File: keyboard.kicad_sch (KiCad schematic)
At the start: 31 parts, among them SW1 SW_PUSH, SW10 SW_PUSH, SW11 SW_PUSH, SW12 SW_PUSH, SW13 SW_PUSH, SW14 SW_PUSH, SW15 SW_PUSH, SW16 SW_PUSH, SW17 SW_PUSH, SW18 SW_PUSH, SW19 SW_PUSH, SW2 SW_PUSH, SW20 SW_PUSH, SW21 SW_PUSH, SW22 SW_PUSH, SW23 SW_PUSH, SW24 SW_PUSH, SW25 SW_PUSH, SW26 SW_PUSH, SW3 SW_PUSH, SW4 SW_PUSH, SW5 SW_PUSH, SW6 SW_PUSH, SW7 SW_PUSH, SW8 SW_PUSH, SW9 SW_PUSH

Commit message: Approximate layout
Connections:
- net SW01L: now also YJT1.2 (P21), YJT2.35 (P19); no longer YJT1.9 (P28), YJT2.9 (P28)
- net SW02L: now also YJT1.14 (P00), YJT2.23 (P09); no longer YJT1.4 (P23), YJT2.4 (P23)
- net SW03L: now also YJT1.20 (P06), YJT2.17 (P03); no longer YJT1.3 (P22), YJT2.3 (P22)
- net SW04L: now also YJT1.26 (P12), YJT2.26 (P12); no longer YJT1.2 (P21), YJT2.2 (P21)
- net SW05L: now also YJT1.3 (P22), YJT2.34 (P18); no longer YJT1.27 (P13), YJT2.27 (P13)
- net SW06L: now also YJT1.15 (P01), YJT2.22 (P08); no longer YJT1.24 (P10), YJT2.24 (P10)
- net SW07L: now also YJT1.21 (P07), YJT2.16 (P02); no longer YJT1.23 (P09), YJT2.23 (P09)
- net SW08L: now also YJT1.27 (P13), YJT2.10 (P29); no longer YJT1.22 (P08), YJT2.22 (P08)
- net SW09L: now also YJT1.4 (P23), YJT2.33 (P17); no longer YJT1.26 (P12), YJT2.26 (P12)
- net SW10L: now also YJT1.16 (P02), YJT2.21 (P07); no longer YJT1.17 (P03), YJT2.17 (P03)
- net SW11L: now also YJT1.22 (P08), YJT2.15 (P01); no longer YJT1.16 (P02), YJT2.16 (P02)
- net SW12L: now also YJT1.28 (P14), YJT2.9 (P28); no longer YJT1.15 (P01), YJT2.15 (P01)
- net SW13L: now also YJT1.9 (P28), YJT2.28 (P14); no longer YJT1.14 (P00), YJT2.14 (P00)
- net SW14L: now also YJT1.17 (P03), YJT2.20 (P06); no longer YJT1.13 (P30), YJT2.13 (P30)
- net SW15L: now also YJT1.23 (P09), YJT2.14 (P00); no longer YJT1.25 (P11), YJT2.25 (P11)
- net SW16L: now also YJT1.29 (P15), YJT2.29 (P15); no longer YJT1.28 (P14), YJT2.28 (P14)
- net SW17L: now also YJT1.10 (P29), YJT2.27 (P13); no longer YJT1.29 (P15), YJT2.29 (P15)
- net SW18L: now also YJT1.18 (P04), YJT2.19 (P05); no longer YJT1.30 (P16), YJT2.30 (P16)
- net SW19L: now also YJT1.24 (P10), YJT2.13 (P30); no longer YJT1.33 (P17), YJT2.33 (P17)
- net SW20L: now also YJT1.30 (P16), YJT2.30 (P16); no longer YJT1.18 (P04), YJT2.18 (P04)
- net SW21L: now also YJT1.13 (P30), YJT2.24 (P10); no longer YJT1.19 (P05), YJT2.19 (P05)
- net SW22L: now also YJT1.19 (P05), YJT2.18 (P04); no longer YJT1.20 (P06), YJT2.20 (P06)
- net SW23L: now also YJT1.25 (P11), YJT2.25 (P11); no longer YJT1.21 (P07), YJT2.21 (P07)
- net SW24L: now also YJT1.33 (P17), YJT2.4 (P23); no longer YJT1.34 (P18), YJT2.34 (P18)
- net SW25L: now also YJT1.34 (P18), YJT2.3 (P22); no longer YJT1.35 (P19), YJT2.35 (P19)
- net SW26L: now also YJT1.35 (P19), YJT2.2 (P21); no longer YJT1.10 (P29), YJT2.10 (P29)

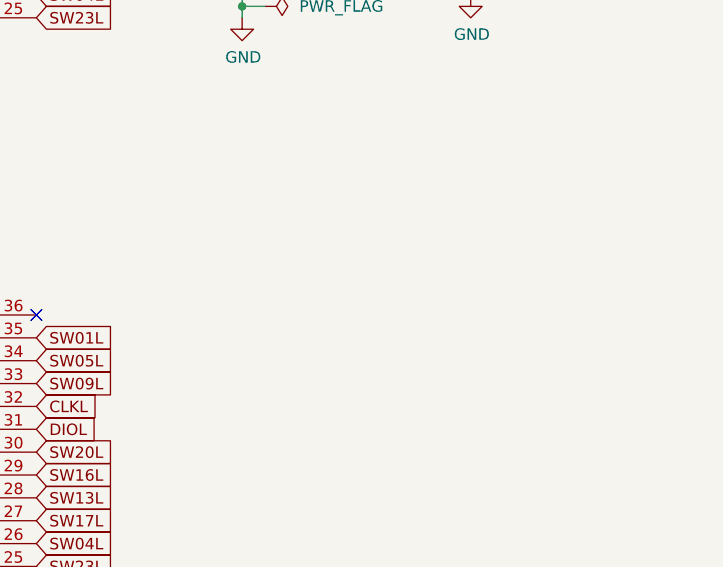
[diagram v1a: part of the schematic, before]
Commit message: Adjust spacing and stagger, add splitkb tenting puck
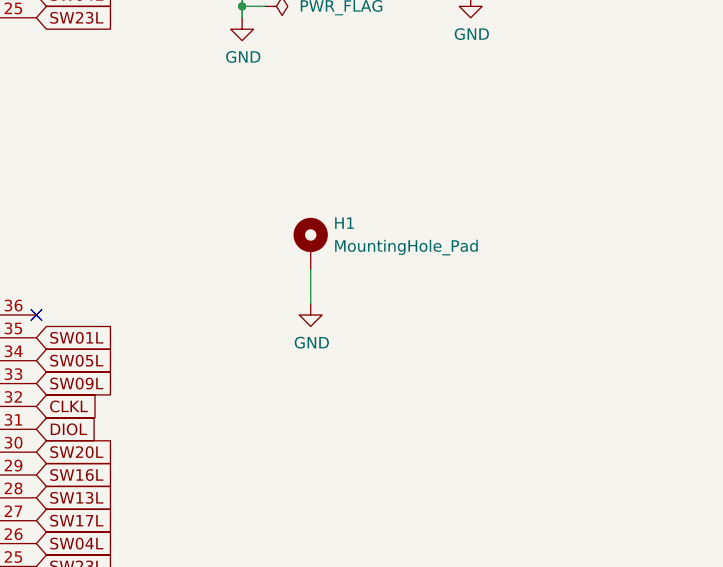
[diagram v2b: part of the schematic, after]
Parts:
- added H1: MountingHole_Pad, keyboard:Tenting_Puck, symbol Mechanical:MountingHole_Pad
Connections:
- net GND: now also H1.1
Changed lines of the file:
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@@
+    (stroke (width 0) (type default))
+  )
+  (wire (pts (xy 226.06 91.44) (xy 226.06 95.25))
     (stroke (width 0) (type default))
   )
@@
     )
   )
+  (symbol (lib_id "power:GND") (at 226.06 95.25 0) (unit 1)
+    (in_bom yes) (on_board yes) (dnp no)
+    (property "Reference" "#PWR039" (at 226.06 101.6 0)
+      (effects (font (size 1.27 1.27)) hide)
+    )
+    (property "Value" "GND" (at 226.187 99.6442 0)
+      (effects (font (size 1.27 1.27)))
+    )
+    (property "Footprint" "" (at 226.06 95.25 0)
+      (effects (font (size 1.27 1.27)) hide)
+    )
+    (property "Datasheet" "" (at 226.06 95.25 0)
+      (effects (font (size 1.27 1.27)) hide)
+    )
+    (pin "1")
+    (instances
+      (project "keyboard"
+        (path "/1164333d-e431-4b47-a8bd-7c7f8608553c"
+          (reference "#PWR039") (unit 1)
+        )
+      )
+    )
+  )
   (symbol (lib_id "power:GND") (at 93.98 115.57 0) (unit 1)
     (in_bom yes) (on_board yes) (dnp no)
@@
         )
       )
+    )
+  )
+  (symbol (lib_id "Mechanical:MountingHole_Pad") (at 226.06 88.9 0) (unit 1)
+    (in_bom yes) (on_board yes) (dnp no) (fields_autoplaced)
+    (property "Reference" "H1" (at 228.6 86.36 0)
+      (effects (font (size 1.27 1.27)) (justify left))
+    )
+    (property "Value" "MountingHole_Pad" (at 228.6 88.9 0)
+      (effects (font (size 1.27 1.27)) (justify left))
+    )
+    (property "Footprint" "keyboard:Tenting_Puck" (at 226.06 88.9 0)
+      (effects (font (size 1.27 1.27)) hide)
+    )
+    (property "Datasheet" "~" (at 226.06 88.9 0)
+      (effects (font (size 1.27 1.27)) hide)
+    )
+    (pin "1")
+    (instances
+      (project "keyboard"
+        (path "/1164333d-e431-4b47-a8bd-7c7f8608553c"
+          (reference "H1") (unit 1)
+        )
+      )

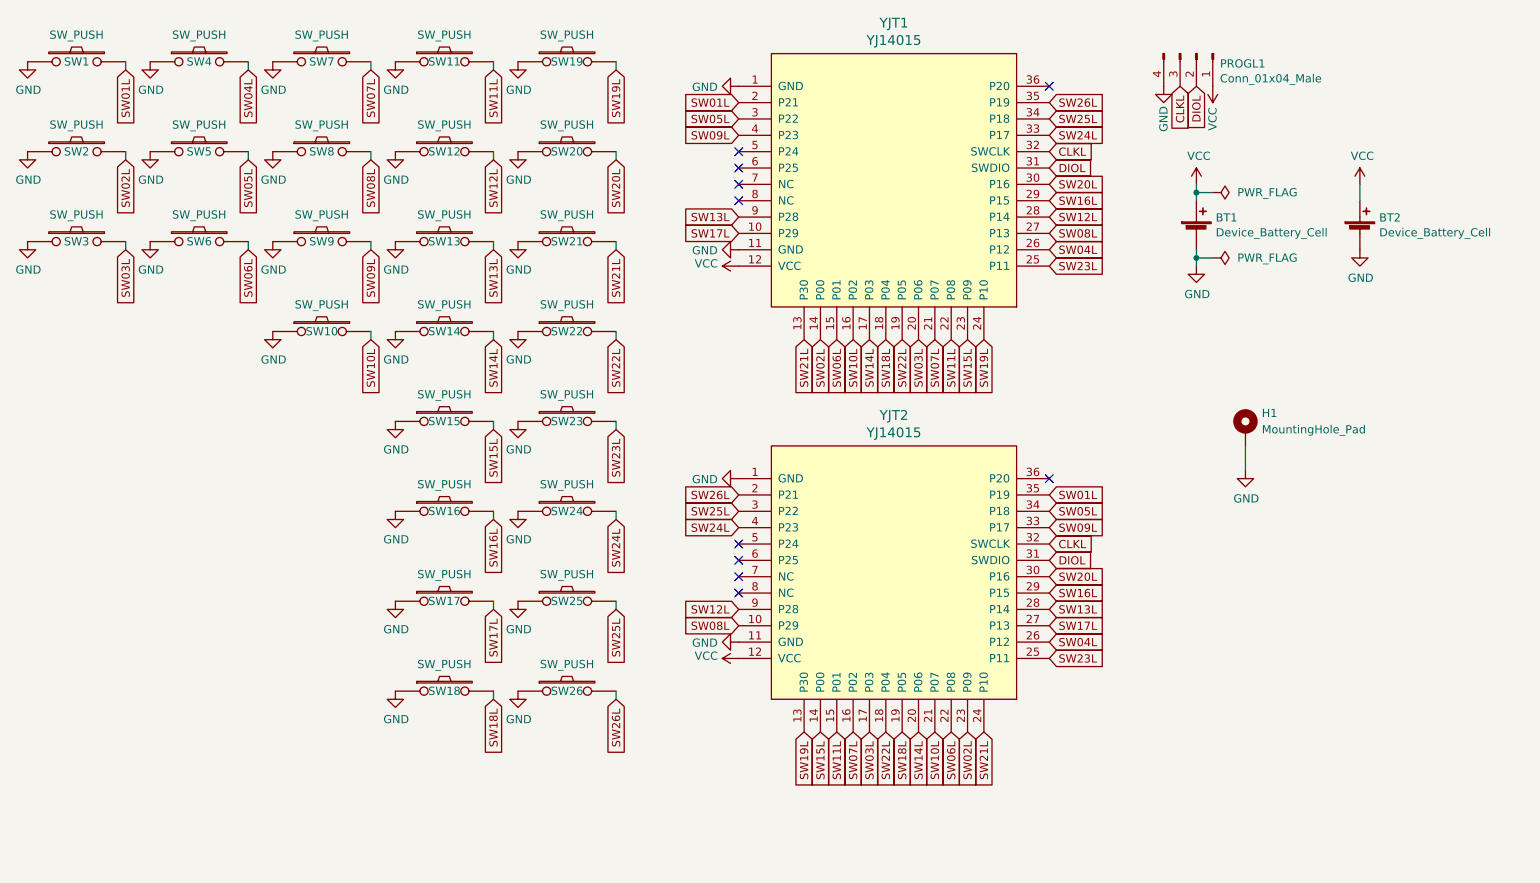
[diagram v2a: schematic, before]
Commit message: fix spacing, add a mod key
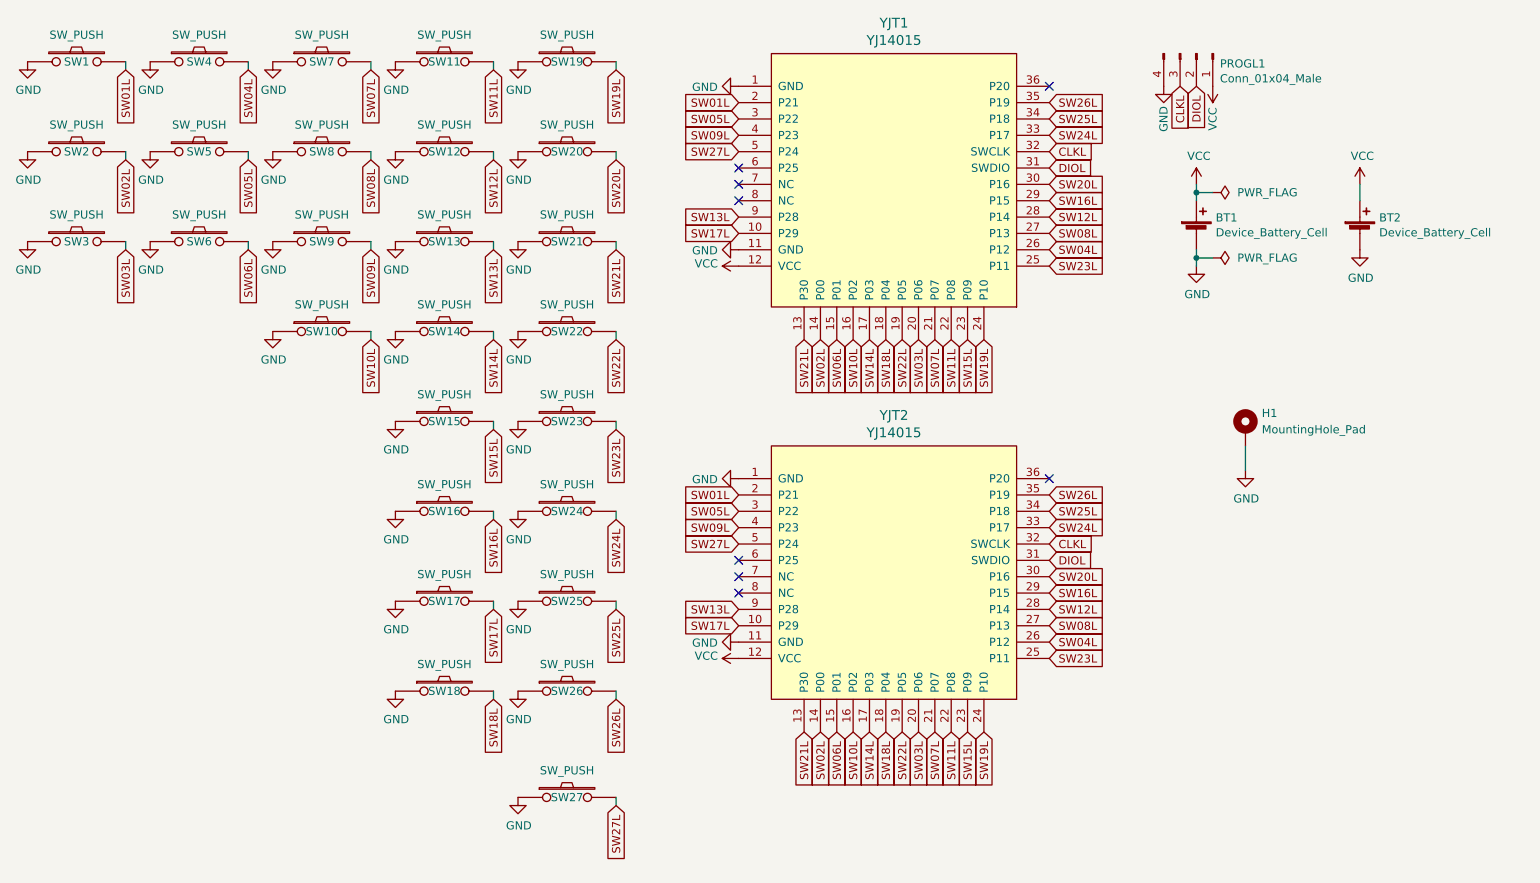
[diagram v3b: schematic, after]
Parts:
- added SW27: SW_PUSH, keyboard:MX_ALPS_PG1350_noLed, symbol keyboard:SW_PUSH
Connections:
- net GND: now also SW27.1
- net SW01L: now also YJT2.2 (P21); no longer YJT2.35 (P19)
- net SW02L: now also YJT2.14 (P00); no longer YJT2.23 (P09)
- net SW03L: now also YJT2.20 (P06); no longer YJT2.17 (P03)
- net SW05L: now also YJT2.3 (P22); no longer YJT2.34 (P18)
- net SW06L: now also YJT2.15 (P01); no longer YJT2.22 (P08)
- net SW07L: now also YJT2.21 (P07); no longer YJT2.16 (P02)
- net SW08L: now also YJT2.27 (P13); no longer YJT2.10 (P29)
- net SW09L: now also YJT2.4 (P23); no longer YJT2.33 (P17)
- net SW10L: now also YJT2.16 (P02); no longer YJT2.21 (P07)
- net SW11L: now also YJT2.22 (P08); no longer YJT2.15 (P01)
- net SW12L: now also YJT2.28 (P14); no longer YJT2.9 (P28)
- net SW13L: now also YJT2.9 (P28); no longer YJT2.28 (P14)
- net SW14L: now also YJT2.17 (P03); no longer YJT2.20 (P06)
- net SW15L: now also YJT2.23 (P09); no longer YJT2.14 (P00)
- net SW17L: now also YJT2.10 (P29); no longer YJT2.27 (P13)
- net SW18L: now also YJT2.18 (P04); no longer YJT2.19 (P05)
- net SW19L: now also YJT2.24 (P10); no longer YJT2.13 (P30)
- net SW21L: now also YJT2.13 (P30); no longer YJT2.24 (P10)
- net SW22L: now also YJT2.19 (P05); no longer YJT2.18 (P04)
- net SW24L: now also YJT2.33 (P17); no longer YJT2.4 (P23)
- net SW25L: now also YJT2.34 (P18); no longer YJT2.3 (P22)
- net SW26L: now also YJT2.35 (P19); no longer YJT2.2 (P21)
- net SW27L: now reaches YJT1.5 (P24)
- net SW27L: now also YJT2.5 (P24), SW27.2
- no-connect marks 10 -> 8
